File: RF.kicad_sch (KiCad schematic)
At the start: 50 parts, among them J1 Conn_Coaxial_Small, J3 RFShield_OnePiece, J5 2.4Ghz Antenna, U2 BGS12WN6E6327, U4 LR1121IMLTRT, Y3 32.768KHz, Y4 32MHz

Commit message: footprint assignment
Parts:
- removed J3: RFShield_OnePiece, symbol Device:RFShield_OnePiece
- C40: footprint Capacitor_SMD:C_0402_1005Metric_Pad0.74x0.62mm_HandSolder -> Capacitor_SMD:C_0603_1608Metric_Pad1.08x0.95mm_HandSolder
- L2: footprint Inductor_SMD:L_0402_1005Metric_Pad0.77x0.64mm_HandSolder -> Inductor_SMD:L_0603_1608Metric_Pad1.05x0.95mm_HandSolder
- Y3: footprint Crystal:Crystal_SMD_0603-2Pin_6.0x3.5mm_HandSoldering -> Crystal:Crystal_SMD_2012-2Pin_2.0x1.2mm_HandSoldering
- Y4: footprint Crystal:Crystal_SMD_0603-2Pin_6.0x3.5mm_HandSoldering -> Crystal:Crystal_SMD_2016-4Pin_2.0x1.6mm

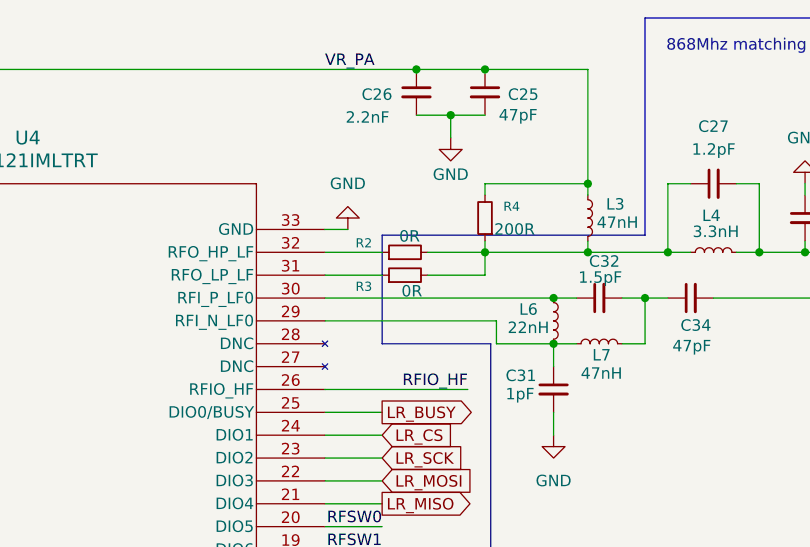
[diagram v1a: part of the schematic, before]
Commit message: RF and initial routing
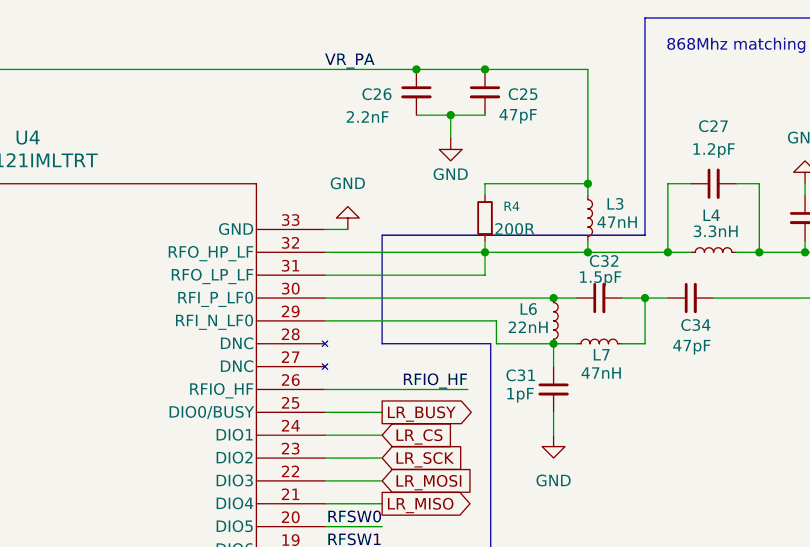
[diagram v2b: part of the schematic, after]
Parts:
- removed R2, R3: 0R, Resistor_SMD:R_0201_0603Metric, symbol Device:R_Small
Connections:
- net at C27.1, L3.2, L4.1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: now also U4.31 (RFO_LP_LF), U4.32 (RFO_HP_LF)
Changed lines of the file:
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@@
 	(wire
 		(pts
-			(xy 130.81 74.93) (xy 137.16 74.93)
+			(xy 130.81 74.93) (xy 148.59 74.93)
 		)
 		(stroke
@@
 	(wire
 		(pts
-			(xy 130.81 72.39) (xy 137.16 72.39)
+			(xy 130.81 72.39) (xy 148.59 72.39)
 		)
 		(stroke
@@
 	(wire
 		(pts
-			(xy 148.59 72.39) (xy 142.24 72.39)
-		)
-		(stroke
-			(width 0)
-			(type default)
-		)
-	)
-	(wire
-		(pts
 			(xy 64.77 87.63) (xy 52.07 87.63)
 		)
@@
 	(wire
 		(pts
-			(xy 142.24 74.93) (xy 148.59 74.93)
-		)
-		(stroke
-			(width 0)
-			(type default)
-		)
-	)
-	(wire
-		(pts
 			(xy 271.78 86.36) (xy 269.24 86.36)
 		)
@@
 	)
 	(symbol
-		(lib_id "Device:R_Small")
-		(at 139.7 72.39 90)
-		(unit 1)
-		(exclude_from_sim no)
-		(in_bom yes)
-		(on_board yes)
-		(dnp no)
-		(property "Reference" "R2"
-			(at 135.128 71.374 90)
-			(effects
-				(font
-					(size 1.016 1.016)
-				)
-			)
-		)
-		(property "Value" "0R"
-			(at 140.208 70.612 90)
-			(effects
-				(font
-					(size 1.27 1.27)
-				)
-			)
-		)
-		(property "Footprint" "Resistor_SMD:R_0201_0603Metric"
-			(at 139.7 72.39 0)
-			(effects
-				(font
-					(size 1.27 1.27)
-				)
-				(hide yes)
-			)
-		)
-		(property "Datasheet" "~"
-			(at 139.7 72.39 0)
-			(effects
-				(font
-					(size 1.27 1.27)
-				)
-				(hide yes)
-			)
-		)
-		(property "Description" "Resistor, small symbol"
-			(at 139.7 72.39 0)
-			(effects
-				(font
-					(size 1.27 1.27)
-				)
-				(hide yes)
-			)
-		)
-		(pin "2"
-		)
-		(pin "1"
-		)
-		(instances
-			(project "lora-stmu535-lr1121-tx"
-				(path "/963238c7-8564-44c5-a128-5d82375c10f7/5e252930-8cb6-4106-8539-d7be2478662a"
-					(reference "R2")
-					(unit 1)
-				)
-			)
-		)
-	)
-	(symbol
 		(lib_id "power:GND")
 		(at 238.125 130.175 0)
@@
 					(unit 1)
 				)
-			)
-		)
-	)
-	(symbol
-		(lib_id "Device:R_Small")
-		(at 139.7 74.93 90)
-		(unit 1)
-		(exclude_from_sim no)
-		(in_bom yes)
-		(on_board yes)
-		(dnp no)
-		(property "Reference" "R3"
-			(at 135.128 76.2 90)
-			(effects
-				(font
-					(size 1.016 1.016)
-				)
-			)
-		)
-		(property "Value" "0R"
-			(at 140.462 76.708 90)
-			(effects
-				(font
-					(size 1.27 1.27)
-				)
-			)
-		)
-		(property "Footprint" "Resistor_SMD:R_0201_0603Metric"
-			(at 139.7 74.93 0)
-			(effects
-				(font
-					(size 1.27 1.27)
-				)
-				(hide yes)
-			)
-		)
-		(property "Datasheet" "~"
-			(at 139.7 74.93 0)
-			(effects
-				(font
-					(size 1.27 1.27)
-				)
-				(hide yes)
-			)
-		)
-		(property "Description" "Resistor, small symbol"
-			(at 139.7 74.93 0)
-			(effects
-				(font
-					(size 1.27 1.27)
-				)
-				(hide yes)
-			)
-		)
-		(pin "2"
-		)
-		(pin "1"
-		)
-		(instances
-			(project "lora-stmu535-lr1121-tx"
-				(path "/963238c7-8564-44c5-a128-5d82375c10f7/5e252930-8cb6-4106-8539-d7be2478662a"
-					(reference "R3")
-					(unit 1)
-				)

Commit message: fix DRC errors and antenna
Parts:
- added L13: 7nH, Inductor_SMD:L_0402_1005Metric_Pad0.77x0.64mm_HandSolder, symbol Device:L_Small
- added L8: 13nH, Inductor_SMD:L_0402_1005Metric_Pad0.77x0.64mm_HandSolder, symbol Device:L_Small
- L9: value 39nH -> 1.3nH; footprint Inductor_SMD:L_0201_0603Metric -> Inductor_SMD:L_0402_1005Metric_Pad0.77x0.64mm_HandSolder
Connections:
- net GND: now also L13.1
- net at L9.2: now also L13.2, L8.1; no longer AE1.1 (A)
- new net: AE1.1 (A), L8.2
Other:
- moved on the sheet: L9

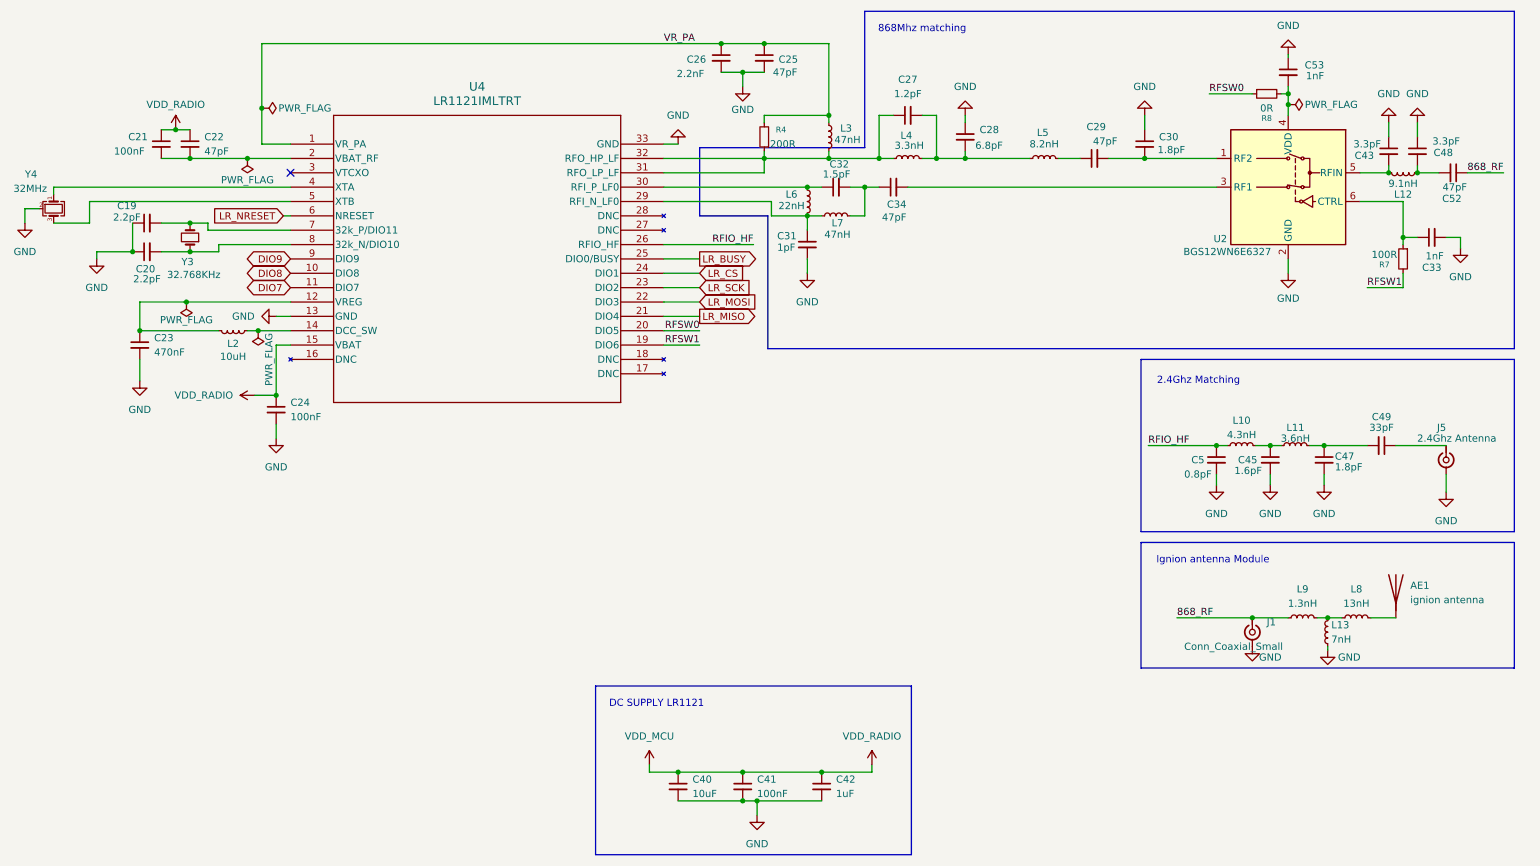
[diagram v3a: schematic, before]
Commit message: changed RF switch in schematics, todo in pcb
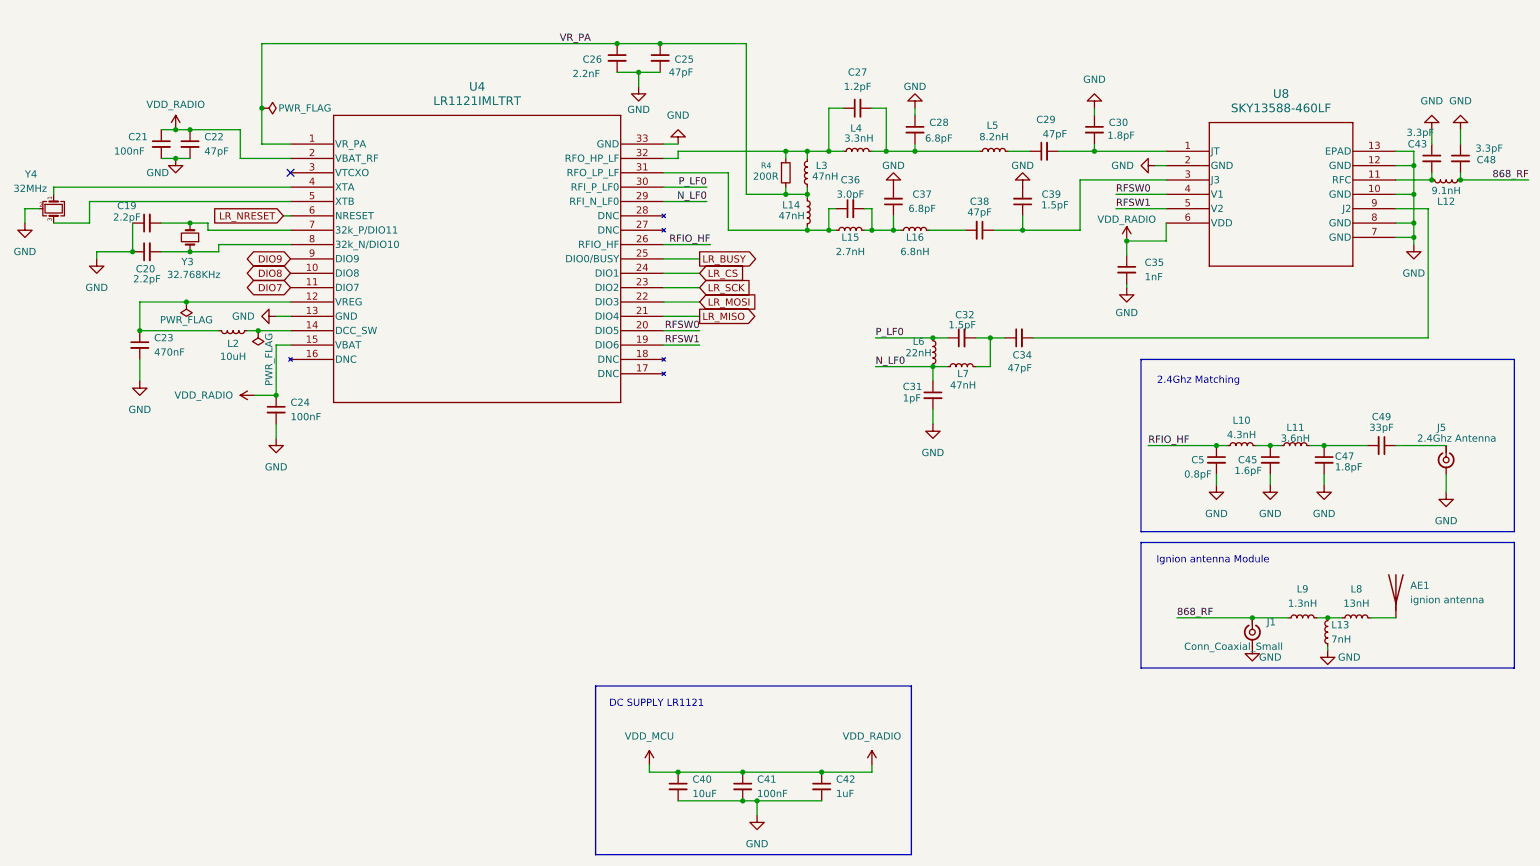
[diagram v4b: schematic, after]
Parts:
- removed C33, C53: 1nF, Capacitor_SMD:C_0201_0603Metric, symbol Device:C_Small
- removed C52: 47pF, Capacitor_SMD:C_0201_0603Metric, symbol Device:C_Small
- removed R7: 100R, Resistor_SMD:R_0201_0603Metric, symbol Device:R_Small
- removed R8: 0R, Resistor_SMD:R_0201_0603Metric, symbol Device:R_Small
- removed U2: BGS12WN6E6327, Package_LGA:Infineon_PG-TSNP-6-10_0.7x1.1mm_0.7x1.1mm_P0.4mm, symbol RF_Switch:BGS12WN6E6327
- added C35: 1nF, Capacitor_SMD:C_0201_0603Metric, symbol Device:C_Small
- added C36: 3.0pF, Capacitor_SMD:C_0201_0603Metric, symbol Device:C_Small
- added C37: 6.8pF, Capacitor_SMD:C_0201_0603Metric, symbol Device:C_Small
- added C38: 47pF, Capacitor_SMD:C_0201_0603Metric, symbol Device:C_Small
- added C39: 1.5pF, Capacitor_SMD:C_0201_0603Metric, symbol Device:C_Small
- added L14: 47nH, Inductor_SMD:L_0201_0603Metric, symbol Device:L_Small
- added L15: 2.7nH, Inductor_SMD:L_0201_0603Metric, symbol Device:L_Small
- added L16: 6.8nH, Inductor_SMD:L_0201_0603Metric, symbol Device:L_Small
- added U8: SKY13588-460LF, sky13588:QFN12_SKY-L, symbol SKY13588:SKY13588-460LF
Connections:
- net 868_RF: now also C48.2, L12.2
- net GND: now also C21.2, C22.2, C35.2, C37.2, C39.2, U8.10 (GND), U8.12 (GND), U8.13 (EPAD), U8.2 (GND), U8.7 (GND), U8.8 (GND)
- net RFSW0: now also U8.4 (V1)
- net RFSW1: now also U8.5 (V2)
- net VDD_MCU: now also U4.2 (VBAT_RF), C35.1, U8.6 (VDD)
- net VR_PA: now also L14.1
- net P_LF0: now reaches C32.1, L6.1, U4.30 (RFI_P_LF0)
- net at C27.1, L3.2, L4.1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: no longer U4.31 (RFO_LP_LF)
- net at C34.2: now also U8.9 (J2)
- net at C43.2, L12.1: now also U8.11 (RFC)
- net at C29.2, C30.2: now also U8.1 (JT)
- net N_LF0: now reaches C31.1, L6.2, L7.1, U4.29 (RFI_N_LF0)
- new net: C36.2, C37.1, L15.2, L16.1
- new net: C38.1, C39.1, U8.3 (J3)
- new net: C38.2, L16.2
- new net: C36.1, L14.2, L15.1, U4.31 (RFO_LP_LF)
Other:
- note removed: "868Mhz matching"
- moved on the sheet: C25, C26, C27, C28, C29, C30, C31, C32, C34, C43, C48, L12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

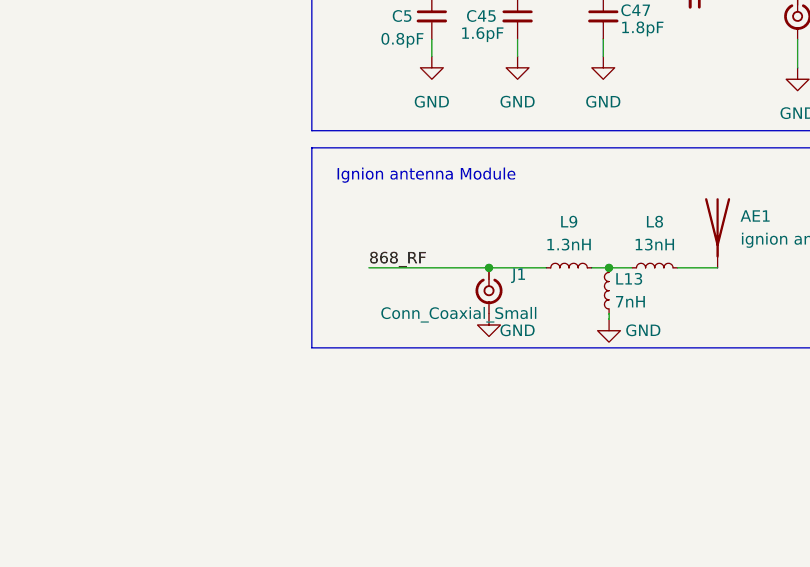
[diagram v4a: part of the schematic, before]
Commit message: separated matching lines
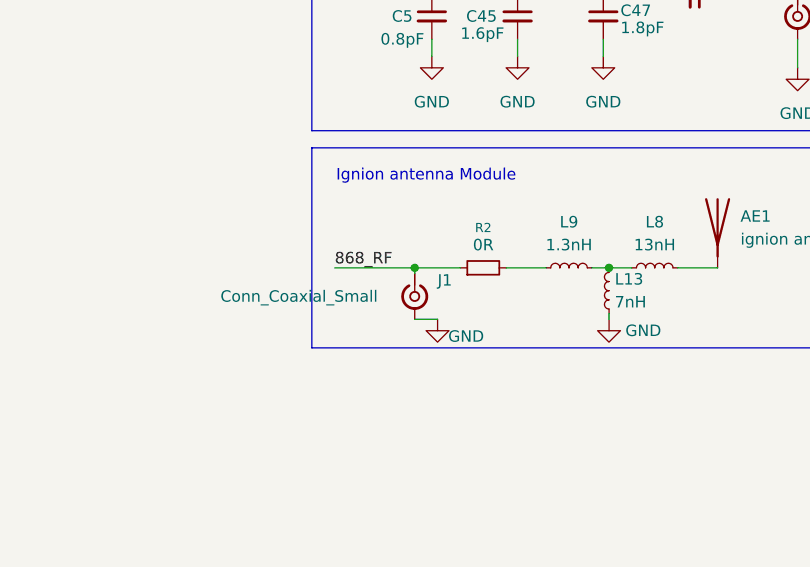
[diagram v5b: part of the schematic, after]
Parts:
- added R2: 0R, Resistor_SMD:R_0603_1608Metric_Pad0.98x0.95mm_HandSolder, symbol Device:R_Small
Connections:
- net 868_RF: now also R2.1; no longer L9.1
- new net: L9.1, R2.2
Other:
- moved on the sheet: J1
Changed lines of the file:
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@@
 	)
 	(junction
-		(at 234.95 153.67)
+		(at 171.45 85.09)
 		(diameter 0)
 		(color 0 0 0 0)
 	)
 	(junction
-		(at 171.45 85.09)
+		(at 263.525 83.82)
 		(diameter 0)
 		(color 0 0 0 0)
 	)
 	(junction
-		(at 263.525 83.82)
+		(at 38.1 102.87)
 		(diameter 0)
 		(color 0 0 0 0)
 	)
 	(junction
-		(at 38.1 102.87)
+		(at 226.695 153.67)
 		(diameter 0)
 		(color 0 0 0 0)
@@
 	(wire
 		(pts
-			(xy 221.615 153.67) (xy 234.95 153.67)
+			(xy 217.805 153.67) (xy 226.695 153.67)
 		)
 		(stroke
@@
 	(wire
 		(pts
+			(xy 226.695 154.305) (xy 226.695 153.67)
+		)
+		(stroke
+			(width 0)
+			(type default)
+		)
+	)
+	(wire
+		(pts
 			(xy 29.21 83.82) (xy 22.86 83.82)
 		)
@@
 	(wire
 		(pts
+			(xy 236.855 153.67) (xy 241.3 153.67)
+		)
+		(stroke
+			(width 0)
+			(type default)
+		)
+	)
+	(wire
+		(pts
 			(xy 167.64 85.09) (xy 171.45 85.09)
 		)
@@
 	(wire
 		(pts
+			(xy 226.695 153.67) (xy 231.775 153.67)
+		)
+		(stroke
+			(width 0)
+			(type default)
+		)
+	)
+	(wire
+		(pts
 			(xy 17.78 81.28) (xy 20.32 81.28)
 		)
@@
 	(wire
 		(pts
-			(xy 234.95 153.67) (xy 241.3 153.67)
-		)
-		(stroke
-			(width 0)
-			(type default)
-		)
-	)
-	(wire
-		(pts
 			(xy 161.29 81.28) (xy 160.02 81.28)
 		)
@@
 	(wire
 		(pts
+			(xy 226.695 159.385) (xy 229.235 159.385)
+		)
+		(stroke
+			(width 0)
+			(type default)
+		)
+	)
+	(wire
+		(pts
 			(xy 188.595 109.22) (xy 186.055 109.22)
 		)
@@
 	)
 	(label "868_RF"
-		(at 221.615 153.67 0)
+		(at 217.805 153.67 0)
 		(effects
 			(font
@@
 	)
 	(symbol
+		(lib_id "Device:R_Small")
+		(at 234.315 153.67 90)
+		(unit 1)
+		(exclude_from_sim no)
+		(in_bom yes)
+		(on_board yes)
+		(dnp no)
+		(property "Reference" "R2"
+			(at 234.315 149.225 90)
+			(effects
+				(font
+					(size 1.016 1.016)
+				)
+			)
+		)
+		(property "Value" "0R"
+			(at 234.315 151.13 90)
+			(effects
+				(font
+					(size 1.27 1.27)
+				)
+			)
+		)
+		(property "Footprint" "Resistor_SMD:R_0603_1608Metric_Pad0.98x0.95mm_HandSolder"
+			(at 234.315 153.67 0)
+			(effects
+				(font
+					(size 1.27 1.27)
+				)
+				(hide yes)
+			)
+		)
+		(property "Datasheet" "~"
+			(at 234.315 153.67 0)
+			(effects
+				(font
+					(size 1.27 1.27)
+				)
+				(hide yes)
+			)
+		)
+		(property "Description" "Resistor, small symbol"
+			(at 234.315 153.67 0)
+			(effects
+				(font
+					(size 1.27 1.27)
+				)
+				(hide yes)
+			)
+		)
+		(pin "1"
+		)
+		(pin "2"
+		)
+		(instances
+			(project "lora-stmu535-lr1121-tx"
+				(path "/963238c7-8564-44c5-a128-5d82375c10f7/5e252930-8cb6-4106-8539-d7be2478662a"
+					(reference "R2")
+					(unit 1)
+				)
+			)
+		)
+	)
+	(symbol
 		(lib_id "Device:C_Small")
 		(at 38.1 105.41 0)
@@
 	(symbol
 		(lib_id "Connector:Conn_Coaxial_Small")
-		(at 234.95 156.21 270)
+		(at 226.695 156.845 270)
 		(unit 1)
 		(exclude_from_sim no)
@@
 		(dnp no)
 		(property "Reference" "J1"
-			(at 237.49 154.4203 90)
+			(at 229.235 155.0553 90)
 			(effects
 				(font
@@
 		)
 		(property "Value" "Conn_Coaxial_Small"
-			(at 222.885 158.75 90)
+			(at 205.105 156.845 90)
 			(effects
 				(font
@@
 		)
 		(property "Footprint" "Connector_Coaxial:U.FL_Molex_MCRF_73412-0110_Vertical"
-			(at 234.95 156.21 0)
+			(at 226.695 156.845 0)
 			(effects
 				(font
@@
 		)
 		(property "Datasheet" "~"
-			(at 234.95 156.21 0)
+			(at 226.695 156.845 0)
 			(effects
 				(font
@@
 		)
 		(property "Description" "small coaxial connector (BNC, SMA, SMB, SMC, Cinch/RCA, LEMO, ...)"
-			(at 234.95 156.21 0)
+			(at 226.695 156.845 0)
 			(effects
 				(font
@@
 	(symbol
 		(lib_id "power:GND")
-		(at 234.95 158.75 0)
+		(at 229.235 159.385 0)
 		(unit 1)
 		(exclude_from_sim no)
@@
 		(dnp no)
 		(property "Reference" "#PWR030"
-			(at 234.95 165.1 0)
+			(at 229.235 165.735 0)
 			(effects
 				(font
@@
 		)
 		(property "Value" "GND"
-			(at 238.125 160.655 0)
+			(at 232.41 161.29 0)
 			(effects
 				(font
@@
 		)
 		(property "Footprint" ""
-			(at 234.95 158.75 0)
+			(at 229.235 159.385 0)
 			(effects
 				(font
@@
 		)
 		(property "Datasheet" ""
-			(at 234.95 158.75 0)
+			(at 229.235 159.385 0)
 			(effects
 				(font
@@
 		)
 		(property "Description" "Power symbol creates a global label with name \"GND\" , ground"
-			(at 234.95 158.75 0)
+			(at 229.235 159.385 0)
 			(effects
 				(font
